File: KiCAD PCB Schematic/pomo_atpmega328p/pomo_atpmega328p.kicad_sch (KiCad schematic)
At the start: 8 parts

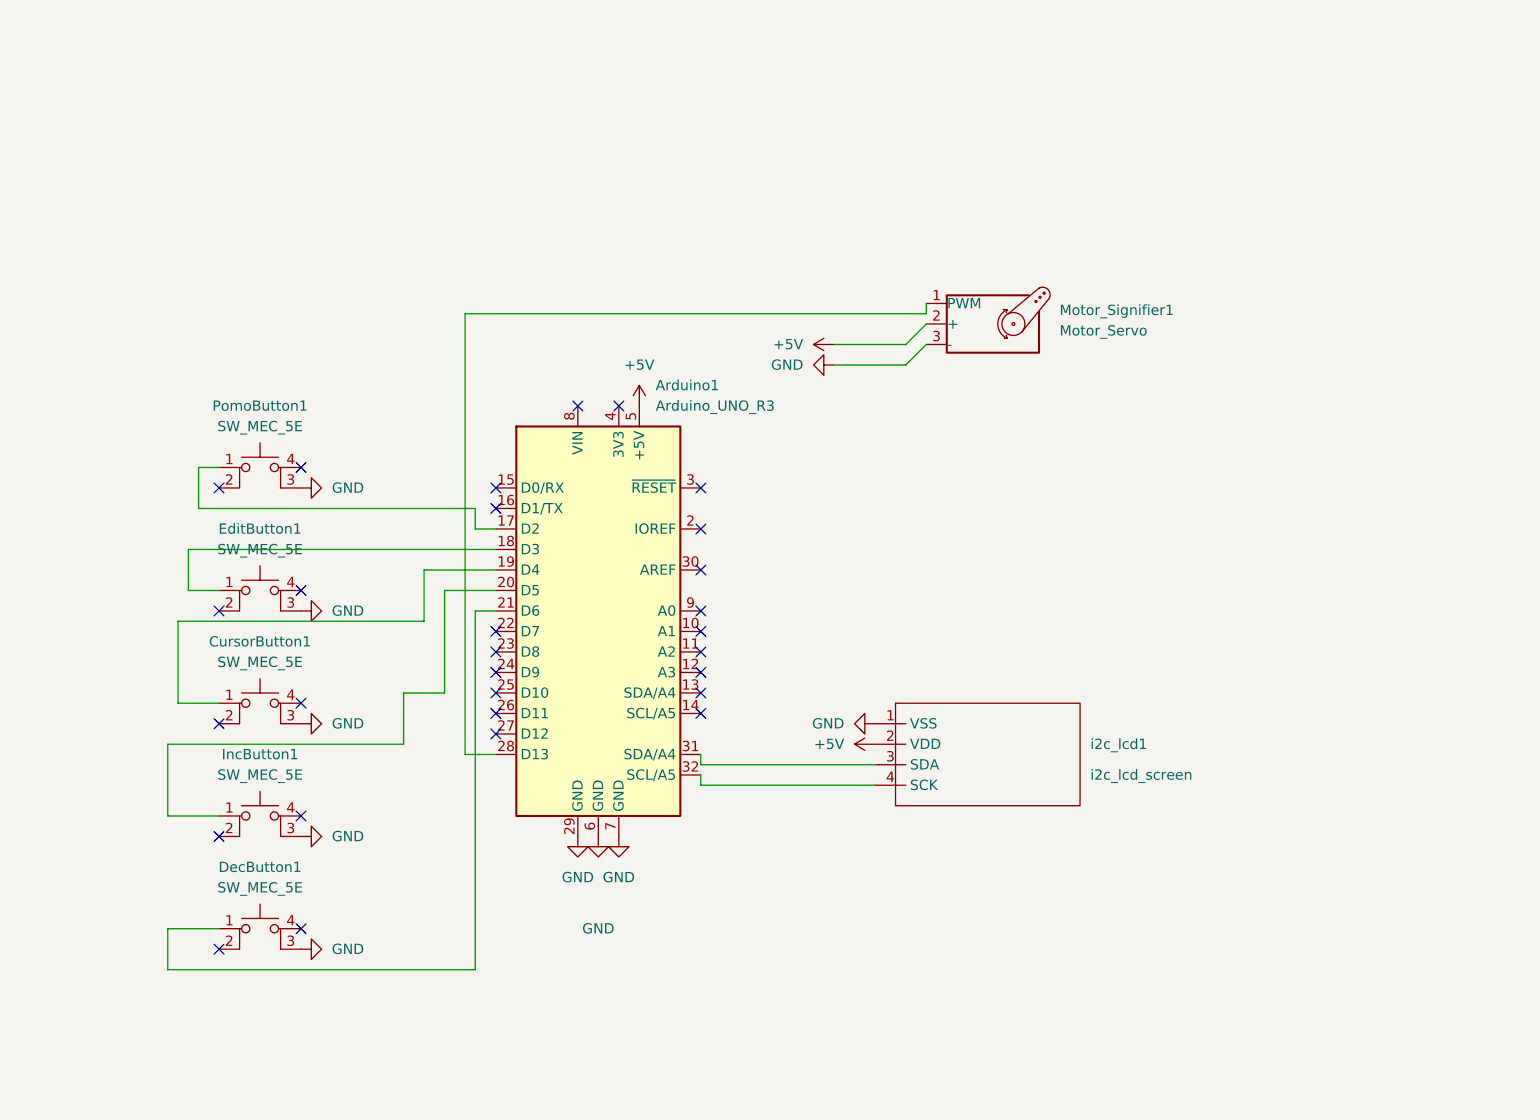
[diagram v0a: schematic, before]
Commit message: Possible atpmega328p alternative
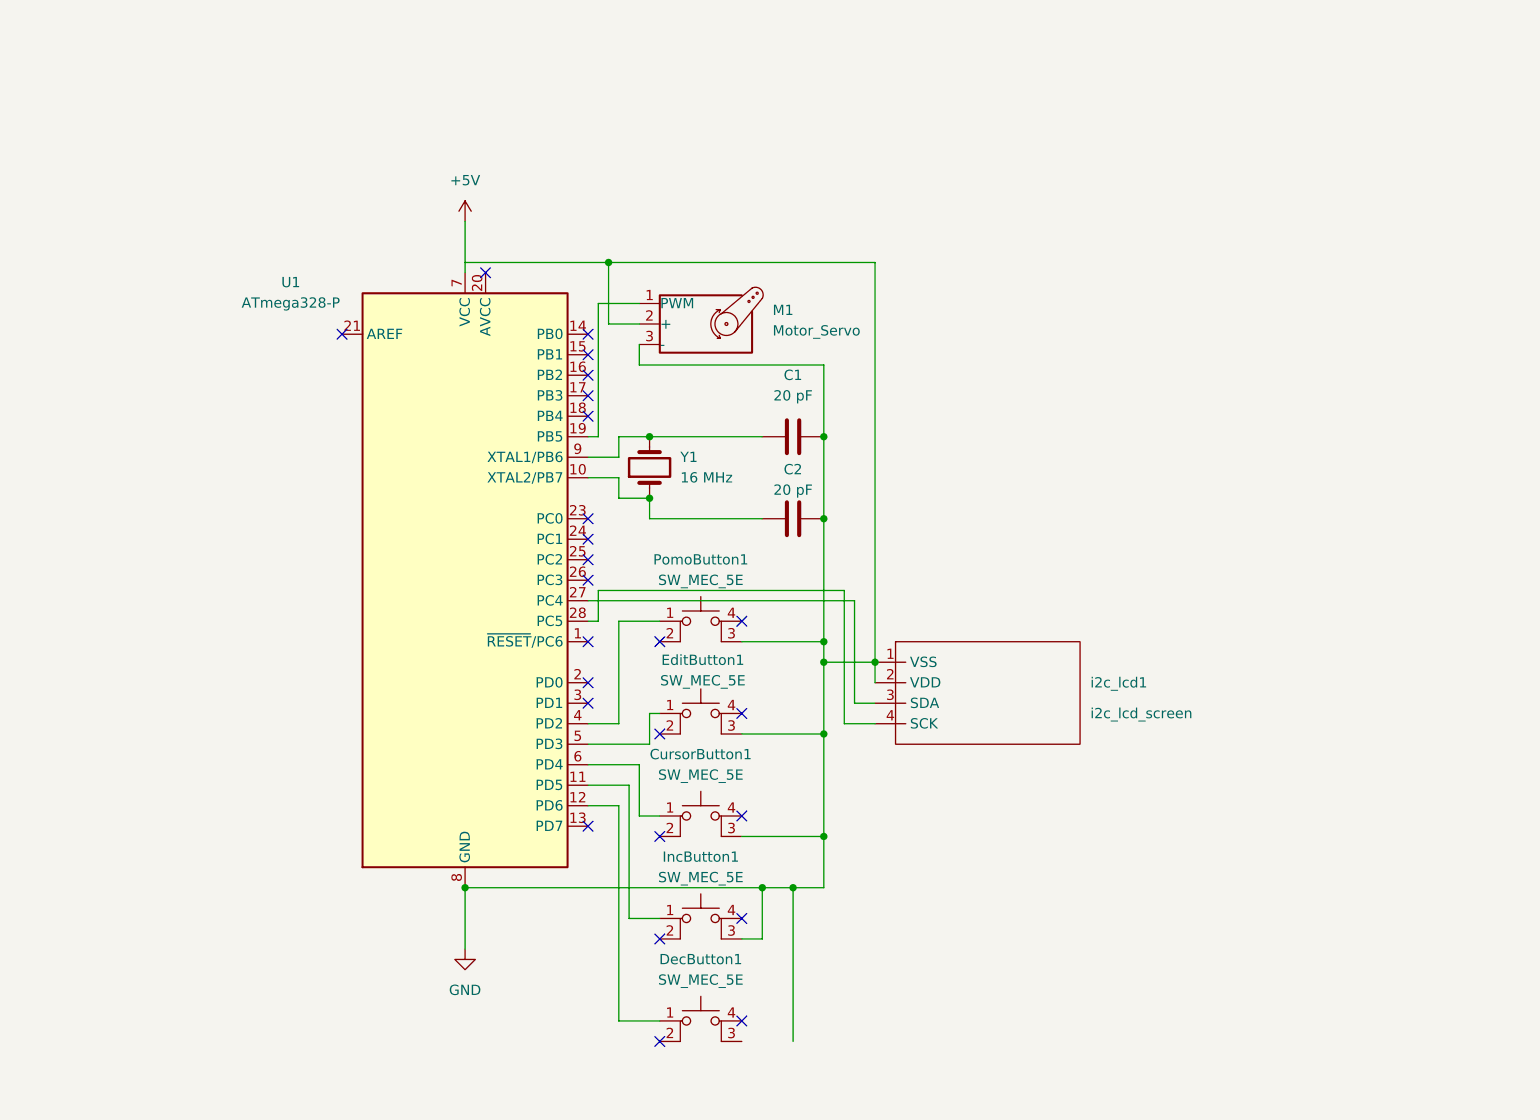
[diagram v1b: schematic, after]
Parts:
- removed Arduino1: Arduino_UNO_R3, Module:Arduino_UNO_R3, symbol MCU_Module:Arduino_UNO_R3
- removed Motor_Signifier1: Motor_Servo, symbol Motor:Motor_Servo
- added C1, C2: 20 pF, symbol Device:C
- added M1: Motor_Servo, symbol Motor:Motor_Servo
- added U1: ATmega328-P, Package_DIP:DIP-28_W7.62mm, symbol MCU_Microchip_ATmega:ATmega328-P
- added Y1: 16 MHz, symbol Device:Crystal
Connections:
- net +5V: now also U1.7 (VCC); no longer i2c_lcd1.2 (VDD)
- net GND: now also i2c_lcd1.2 (VDD), C1.1, C2.2, M1.2 (+), M1.3 (-), U1.22 (GND), U1.8 (GND); no longer DecButton1.3 (K)
- net at CursorButton1.1: now also U1.6 (PD4)
- net at i2c_lcd1.3 (SDA): now also U1.27 (PC4)
- net at i2c_lcd1.4 (SCK): now also U1.28 (PC5)
- net at DecButton1.1: now also U1.12 (PD6)
- net at PomoButton1.1: now also U1.4 (PD2)
- net at EditButton1.1: now also U1.5 (PD3)
- net at IncButton1.1: now also U1.11 (PD5)
- new net: C2.1, U1.10 (XTAL2/PB7), Y1.1
- new net: C1.2, U1.9 (XTAL1/PB6), Y1.2
- new net: M1.1 (PWM), U1.19 (PB5)
- no-connect marks 29 -> 25

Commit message: Redone ATPmega328p Schematic, need traces properly placed and schematic consider having decoup caps
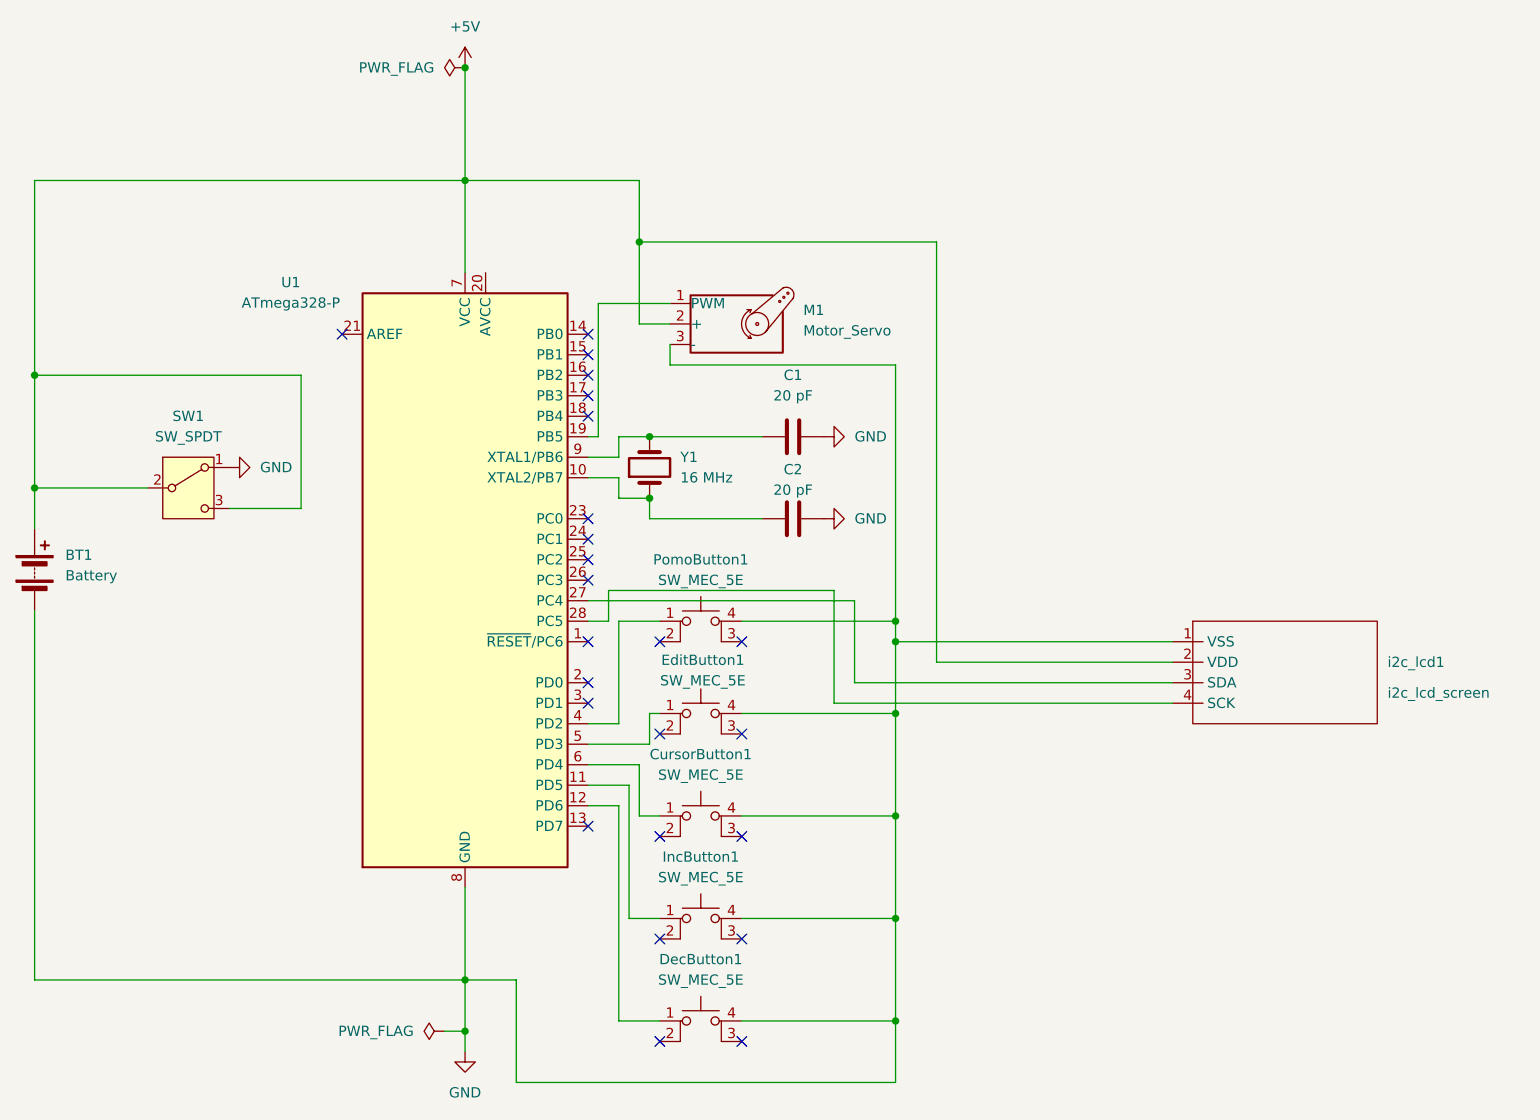
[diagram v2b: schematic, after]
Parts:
- added BT1: Battery, Battery:BatteryHolder_Keystone_2468_2xAAA, symbol Device:Battery
- added SW1: SW_SPDT, symbol Switch:SW_SPDT
- C1, C2: footprint (none) -> Capacitor_THT:C_Disc_D5.0mm_W2.5mm_P5.00mm
- CursorButton1, DecButton1, EditButton1, IncButton1: footprint (none) -> Button_Switch_THT:SW_PUSH-12mm
- M1: footprint (none) -> Connector_PinHeader_2.54mm:PinHeader_1x03_P2.54mm_Vertical
- PomoButton1: footprint (none) -> Button_Switch_THT:SW_PUSH_6mm
- Y1: footprint (none) -> Crystal:Crystal_HC18-U_Vertical
- i2c_lcd1: footprint (none) -> Connector_PinSocket_2.54mm:PinSocket_1x04_P2.54mm_Horizontal
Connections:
- net +5V: now also M1.2 (+), i2c_lcd1.2 (VDD), BT1.1 (+), SW1.2 (B), SW1.3 (C)
- net GND: now also CursorButton1.4 (A), DecButton1.4 (A), EditButton1.4 (A), IncButton1.4 (A), PomoButton1.4 (A), BT1.2 (-), SW1.1 (A); no longer CursorButton1.3 (K), EditButton1.3 (K), IncButton1.3 (K), M1.2 (+), PomoButton1.3 (K), i2c_lcd1.2 (VDD)
- no-connect marks 25 -> 24
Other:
- moved on the sheet: M1, i2c_lcd1
